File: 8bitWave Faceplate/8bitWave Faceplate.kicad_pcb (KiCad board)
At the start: 2 copper layers, 99.7 x 64.1 mm, 51 parts, among them IC1 0.96_I2C_OLED, J1 I2C_VOL, J2 SPI, J3 EXTENSION, M1 Mounting, M2 Mounting, M3 Mounting, M4 Mounting, U1 74HC595_ALT, U2 74HC595_ALT

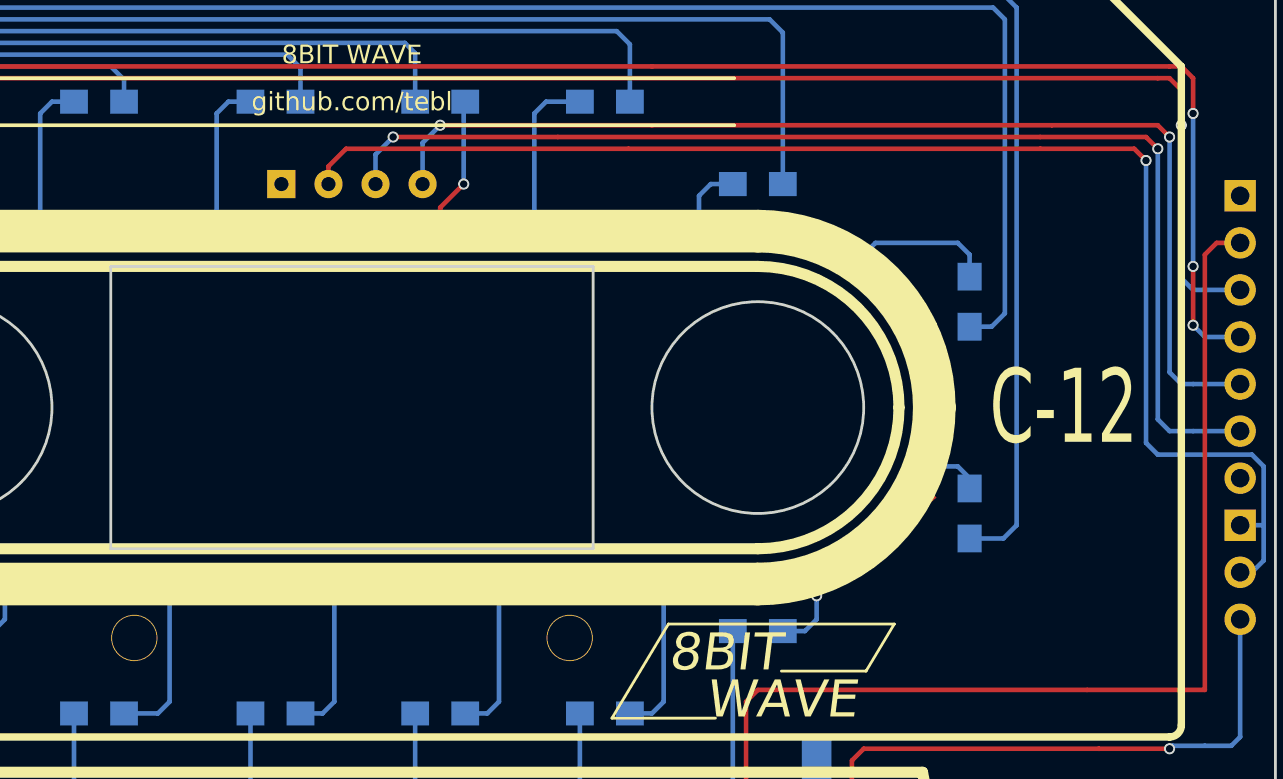
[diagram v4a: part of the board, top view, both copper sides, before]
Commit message: Allow faceplate to choose OLED pin order
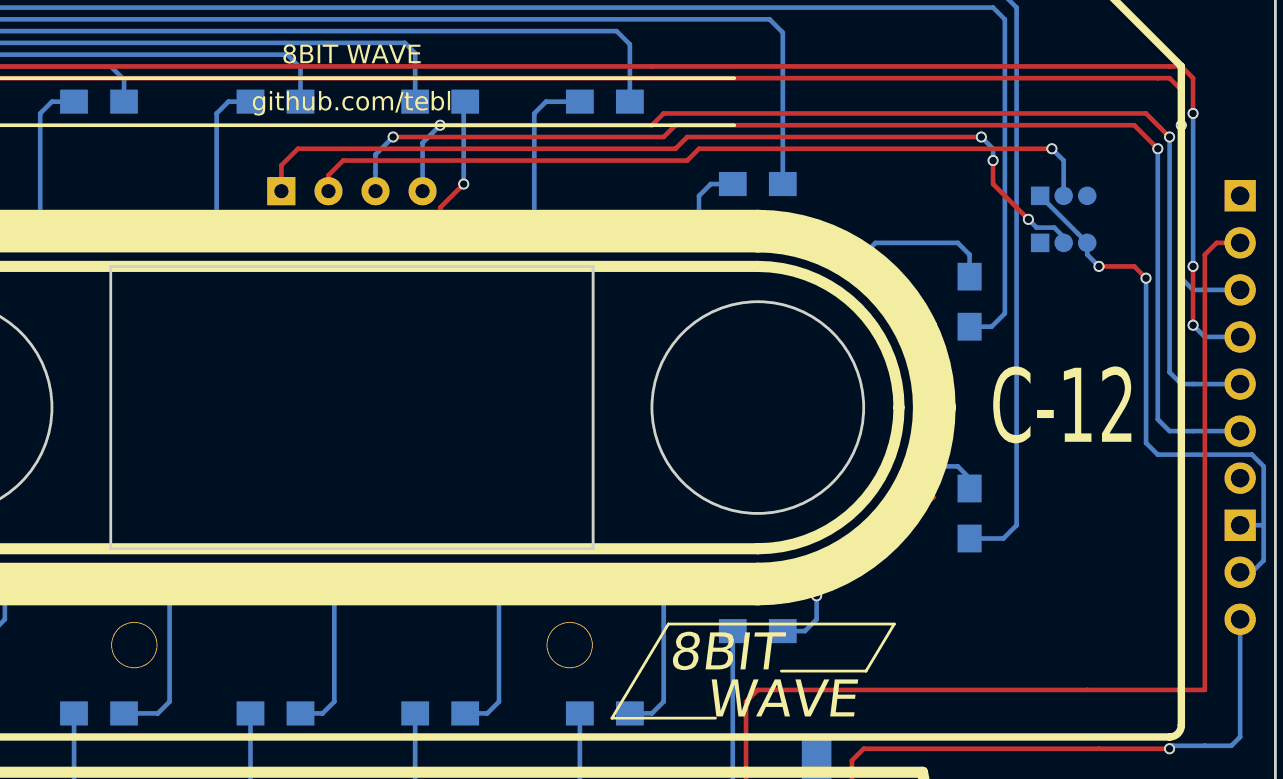
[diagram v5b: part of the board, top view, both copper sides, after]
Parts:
- added JP1: PIN2_VCC, wire_pads:OLED_SEL, B.Cu at (157.5, 95.2)
- added JP2: PIN1_GND, wire_pads:OLED_SEL, B.Cu at (157.5, 97.8)
- moved IC1 0.39 mm to (120.3, 95.0)
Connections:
- IC1 pad 1: GND -> Net-(IC1-Pad1)
- IC1 pad 2: VCC -> Net-(IC1-Pad2)
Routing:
- net Net-(IC1-Pad1): track 0.00 -> 47.5 mm, vias 0 -> 3
- net VCC: track 75.1 -> 31.6 mm, vias 1 -> 2
- net Net-(IC1-Pad2): track 0.00 -> 42.9 mm, vias 0 -> 1
- net /SCL: track 63.1 -> 64.7 mm
- net /SDA: track 59.3 -> 60.9 mm
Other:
- board text added: "JP1/JP2: Link 1-2 when OLED pin 1 is GND, 3-4 if VCC"
